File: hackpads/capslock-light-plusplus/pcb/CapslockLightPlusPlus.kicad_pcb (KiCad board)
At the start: 2 copper layers, 80 x 65 mm, 24 parts, among them J0 Conn_01x03_Socket, J1 Conn_01x04, SW0 SW_Push, SW1 SW_Push, SW2 SW_Push, SW3 SW_Push, SW4 SW_Push, SW5 SW_Push, SW6 RotaryEncoder_Switch_MP, SW7 SW_Push, SW8 SW_Push, U0 Seeed Studio XIAO SAMD21

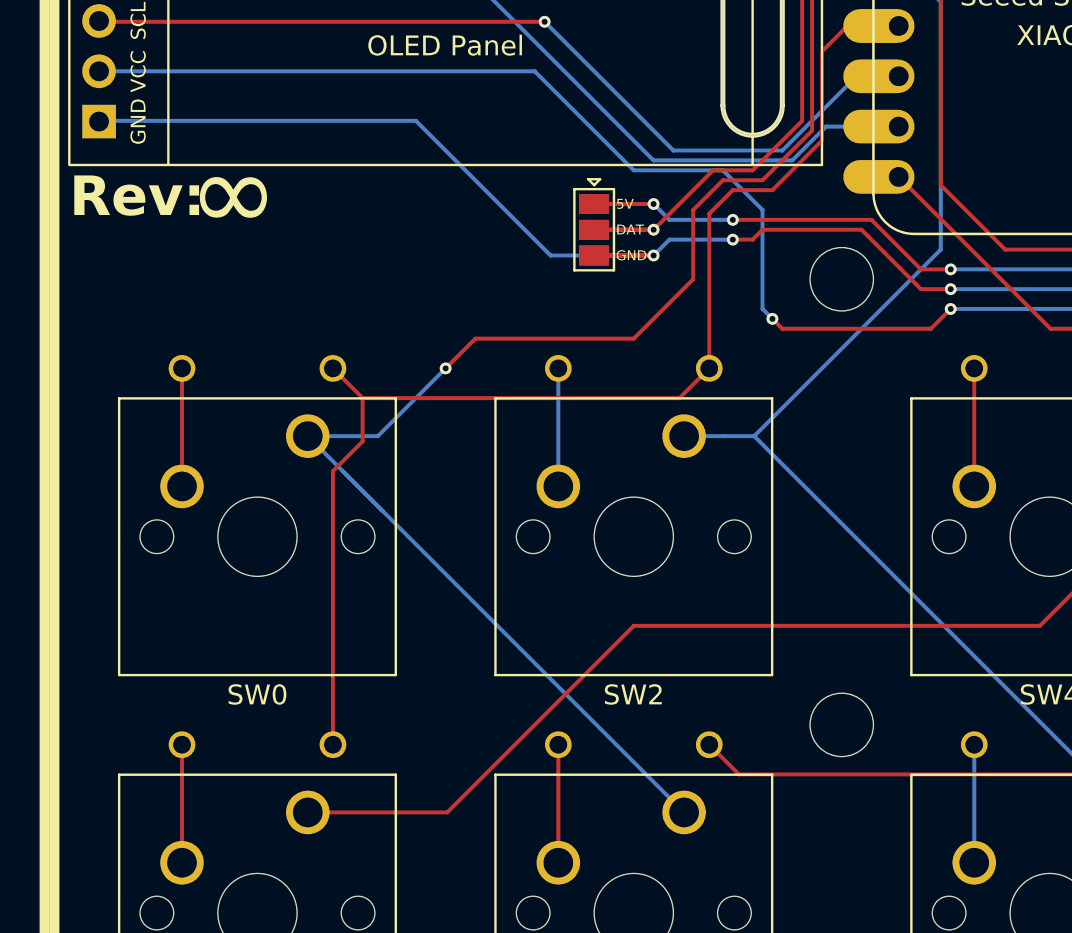
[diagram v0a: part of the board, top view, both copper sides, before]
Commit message: Minior changes to the pcb to remove SMD pads, OLED changes
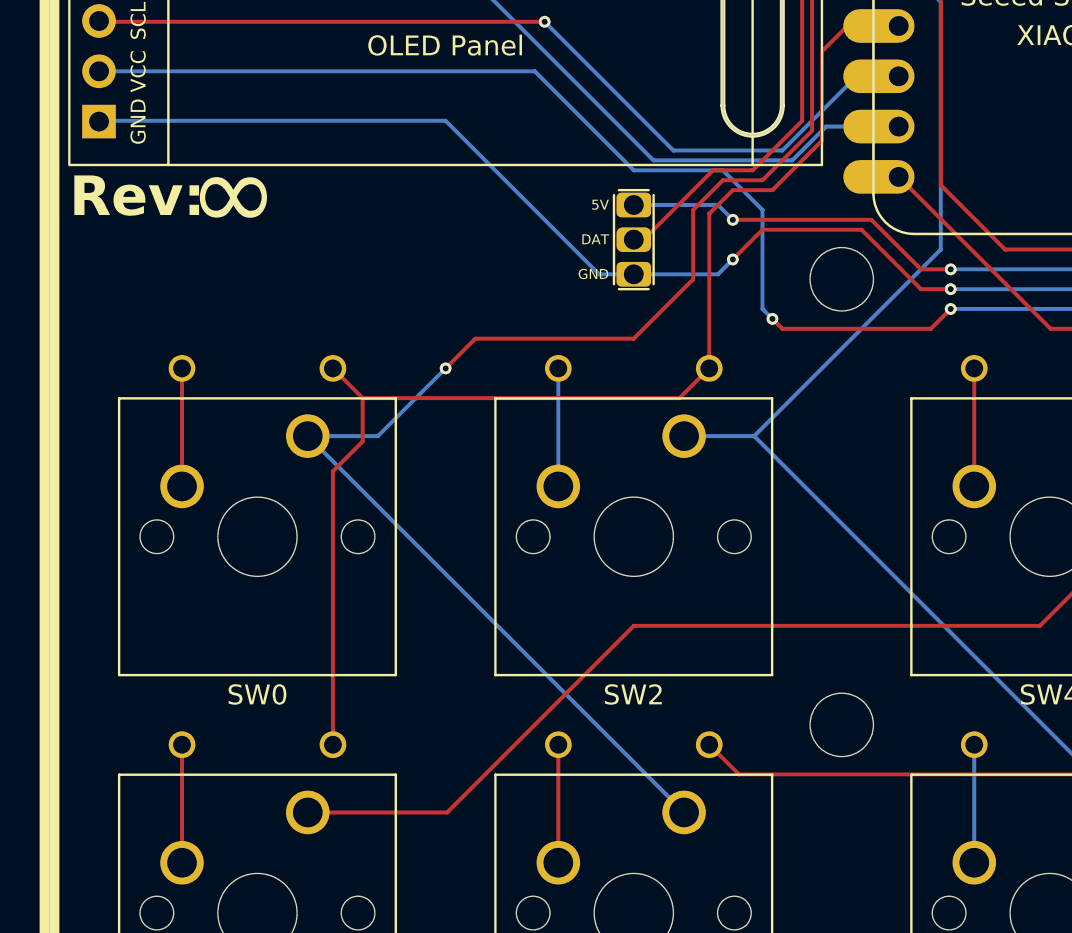
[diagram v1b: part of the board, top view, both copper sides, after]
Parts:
- removed the J0 at (75.5, 43.5)
- moved J0 2.06 mm to (77.5, 44.0)
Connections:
- net Net-(J0-Pin_2) renamed /DAT
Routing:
- net /DAT: track 31.9 -> 26.6 mm, vias 1 -> 0
- net /5V: track 51.6 -> 46.6 mm, vias 3 -> 2
- net C1: track 116.1 -> 113.3 mm
- net GND: track 105.9 -> 103.7 mm, vias 3 -> 2
